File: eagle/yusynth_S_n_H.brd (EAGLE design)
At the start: 100.8 x 81 mm, 43 parts, among them IC1 TL074P, IC2 TL071P, Q1 BF245, T1 2N3904

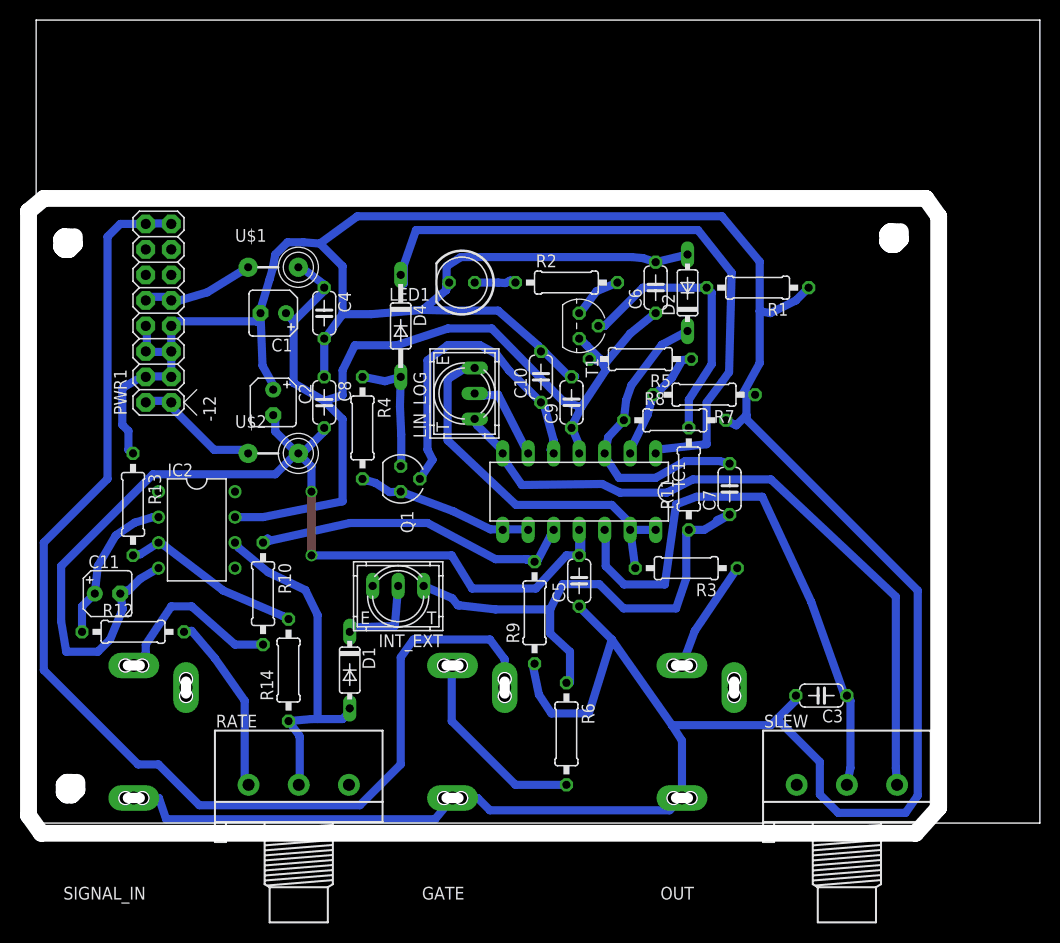
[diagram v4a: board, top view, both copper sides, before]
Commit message: adjusted a spacing, removed ridiculous bus gate and corrected pot reversals
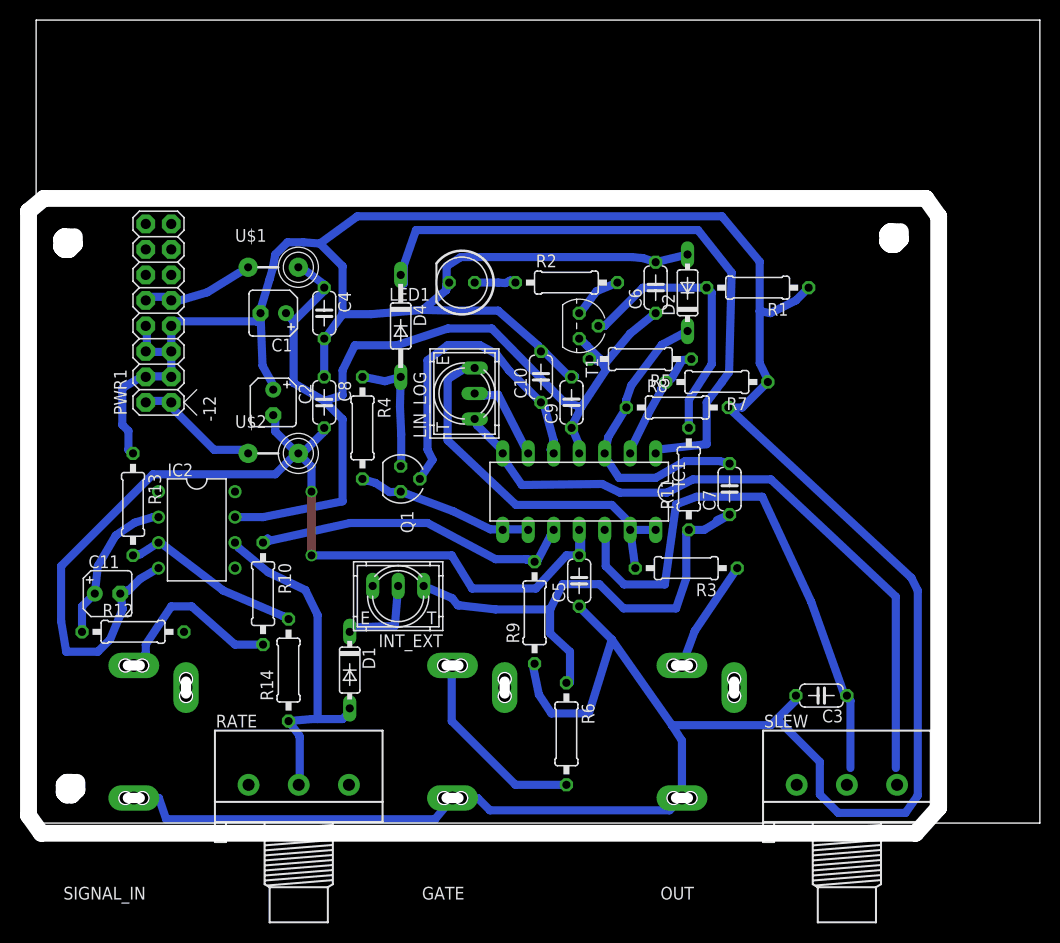
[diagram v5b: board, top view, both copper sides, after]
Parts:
- moved R7 1.80 mm to (67.8, 43.9)
- moved R8 1.30 mm to (63.9, 41.4)
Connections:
- removed net N$24: R12.2, RATE.1
- net N$12: now also R12.2, RATE.3; no longer GATE.P$2, PWR1.15, PWR1.16
- net N$19: now also SLEW.1; no longer SLEW.3
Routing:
- net N$12: track 121.3 -> 0.00 mm
- net N$24: track 18.0 -> 0.00 mm
- net N$13: track 57.7 -> 56.0 mm
- net N$19: track 69.5 -> 67.8 mm
- net N$7: track 11.8 -> 13.3 mm
- net GND: track 374.0 -> 372.6 mm
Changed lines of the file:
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@@
 <element name="R5" library="rcl" package="0207/10" value="100k" x="60.198" y="46.228" rot="R180"/>
 <element name="R6" library="rcl" package="0207/10" value="1k" x="52.832" y="8.89" rot="R270"/>
-<element name="R7" library="rcl" package="0207/10" value="10k" x="66.548" y="42.672" rot="R180"/>
-<element name="R8" library="rcl" package="0207/10" value="100k" x="63.627" y="40.132"/>
+<element name="R7" library="rcl" package="0207/10" value="10k" x="67.818" y="43.942" rot="R180"/>
+<element name="R8" library="rcl" package="0207/10" value="100k" x="63.881" y="41.402"/>
 <element name="R9" library="rcl" package="0207/10" value="100k" x="49.657" y="20.955" rot="R90"/>
 <element name="SLEW" library="pot" package="3RP/1610N" value="1M log" x="80.772" y="3.81"/>
@@
 <wire x1="28.2702" y1="57.7342" x2="26.6192" y2="57.8612" width="0.8128" layer="16"/>
 <wire x1="30.5308" y1="50.6984" x2="30.5308" y2="55.4736" width="0.8128" layer="16"/>
-<wire x1="70.4088" y1="42.7736" x2="72.0852" y2="45.8216" width="0.8128" layer="16"/>
-<wire x1="70.4088" y1="42.7736" x2="71.628" y2="42.672" width="0.8128" layer="16"/>
+<wire x1="72.9488" y1="44.0436" x2="72.0852" y2="45.8216" width="0.8128" layer="16"/>
+<wire x1="72.9488" y1="44.0436" x2="72.898" y2="43.942" width="0.8128" layer="16"/>
 <wire x1="63.3476" y1="9.7536" x2="57.3532" y2="18.288" width="0.8128" layer="16"/>
 <wire x1="57.3532" y1="18.288" x2="54.3052" y2="21.336" width="0.8128" layer="16"/>
@@
 <wire x1="55.0672" y1="10.922" x2="51.3334" y2="10.922" width="0.8128" layer="16"/>
 <wire x1="57.3532" y1="18.288" x2="55.0672" y2="10.922" width="0.8128" layer="16"/>
-<wire x1="70.7644" y1="40.2336" x2="70.7644" y2="40.64" width="0.8128" layer="16"/>
-<wire x1="70.7644" y1="40.64" x2="70.7644" y2="42.672" width="0.8128" layer="16"/>
-<wire x1="87.8332" y1="23.1648" x2="70.7644" y2="40.2336" width="0.8128" layer="16"/>
 <wire x1="87.8332" y1="2.7432" x2="87.8332" y2="23.1648" width="0.8128" layer="16"/>
 <wire x1="86.614" y1="1.016" x2="87.8332" y2="2.7432" width="0.8128" layer="16"/>
@@
 <wire x1="78.0796" y1="6.096" x2="78.0796" y2="2.8448" width="0.8128" layer="16"/>
 <wire x1="73.8124" y1="10.3632" x2="78.0796" y2="6.096" width="0.8128" layer="16"/>
-<wire x1="70.7644" y1="42.672" x2="71.628" y2="42.672" width="0.8128" layer="16"/>
 <wire x1="40.8432" y1="53.086" x2="40.8432" y2="53.594" width="0.8128" layer="16"/>
 <wire x1="40.8432" y1="53.594" x2="40.894" y2="53.6448" width="0.8128" layer="16"/>
@@
 <wire x1="68.326" y1="60.452" x2="32.004" y2="60.452" width="0.8128" layer="16"/>
 <wire x1="32.004" y1="60.452" x2="28.2702" y2="57.7342" width="0.8128" layer="16"/>
-<wire x1="68.707" y1="40.132" x2="69.7484" y2="39.624" width="0.8128" layer="16"/>
-<wire x1="69.7484" y1="39.624" x2="70.7644" y2="40.64" width="0.8128" layer="16"/>
+<wire x1="87.8332" y1="23.1648" x2="87.1982" y2="24.4348" width="0.8128" layer="16"/>
+<wire x1="87.1982" y1="24.4348" x2="68.961" y2="41.402" width="0.8128" layer="16"/>
 <wire x1="49.4538" y1="15.8496" x2="49.657" y2="15.875" width="0" layer="19" extent="16-16"/>
-</signal>
-<signal name="N$12">
-<contactref element="GATE" pad="P$2"/>
-<contactref element="PWR1" pad="15"/>
-<contactref element="PWR1" pad="16"/>
-<wire x1="13.462" y1="59.7408" x2="11.0236" y2="59.7408" width="0.8128" layer="16"/>
-<wire x1="11.0236" y1="59.7408" x2="10.922" y2="59.69" width="0.8128" layer="16"/>
-<wire x1="13.462" y1="59.7408" x2="13.462" y2="59.69" width="0.8128" layer="16"/>
-<wire x1="46.682" y1="13.5" x2="46.682" y2="16.31" width="0.8128" layer="16"/>
-<wire x1="46.682" y1="16.31" x2="45.212" y2="18.288" width="0.8128" layer="16"/>
-<wire x1="45.212" y1="18.288" x2="37.592" y2="18.288" width="0.8128" layer="16"/>
-<wire x1="37.592" y1="18.288" x2="36.322" y2="16.51" width="0.8128" layer="16"/>
-<wire x1="36.322" y1="16.51" x2="36.322" y2="5.842" width="0.8128" layer="16"/>
-<wire x1="36.322" y1="5.842" x2="32.258" y2="1.778" width="0.8128" layer="16"/>
-<wire x1="32.258" y1="1.778" x2="16.256" y2="1.778" width="0.8128" layer="16"/>
-<wire x1="16.256" y1="1.778" x2="12.192" y2="5.842" width="0.8128" layer="16"/>
-<wire x1="12.192" y1="5.842" x2="10.16" y2="5.842" width="0.8128" layer="16"/>
-<wire x1="10.16" y1="5.842" x2="0.762" y2="15.24" width="0.8128" layer="16"/>
-<wire x1="0.762" y1="15.24" x2="0.762" y2="27.94" width="0.8128" layer="16"/>
-<wire x1="0.762" y1="27.94" x2="7.112" y2="34.29" width="0.8128" layer="16"/>
-<wire x1="7.112" y1="34.29" x2="7.112" y2="58.42" width="0.8128" layer="16"/>
-<wire x1="7.112" y1="58.42" x2="8.382" y2="59.69" width="0.8128" layer="16"/>
-<wire x1="8.382" y1="59.69" x2="10.922" y2="59.69" width="0.8128" layer="16"/>
+<wire x1="68.961" y1="41.402" x2="70.358" y2="41.402" width="0.8128" layer="16"/>
+<wire x1="70.358" y1="41.402" x2="72.898" y2="43.942" width="0.8128" layer="16"/>
 </signal>
 <signal name="N$14">
@@
 <wire x1="59.182" y1="37.1348" x2="59.182" y2="36.83" width="0.8128" layer="16"/>
 <wire x1="60.9092" y1="40.64" x2="59.182" y2="37.1348" width="0.8128" layer="16"/>
-<wire x1="60.9092" y1="40.64" x2="61.468" y2="42.672" width="0.8128" layer="16"/>
+<wire x1="60.9092" y1="40.64" x2="62.738" y2="43.942" width="0.8128" layer="16"/>
 <wire x1="63.3476" y1="44.3484" x2="64.3636" y2="46.1264" width="0.8128" layer="16"/>
 <wire x1="62.2808" y1="43.2816" x2="63.3476" y2="44.3484" width="0.8128" layer="16"/>
 <wire x1="64.3636" y1="46.1264" x2="65.278" y2="46.228" width="0.8128" layer="16"/>
-<wire x1="62.2808" y1="43.2816" x2="61.468" y2="42.672" width="0.8128" layer="16"/>
+<wire x1="62.2808" y1="43.2816" x2="62.738" y2="43.942" width="0.8128" layer="16"/>
 </signal>
 <signal name="N$5">
@@
 <wire x1="56.9976" y1="38.4556" x2="56.7436" y2="37.1856" width="0.8128" layer="16"/>
 <wire x1="56.7436" y1="37.1856" x2="56.642" y2="36.83" width="0.8128" layer="16"/>
-<wire x1="56.9976" y1="38.4556" x2="58.547" y2="40.132" width="0.8128" layer="16"/>
+<wire x1="56.9976" y1="38.4556" x2="58.801" y2="41.402" width="0.8128" layer="16"/>
 <wire x1="64.6684" y1="36.068" x2="68.072" y2="36.068" width="0.8128" layer="16"/>
 <wire x1="61.722" y1="34.3916" x2="64.6684" y2="36.068" width="0.8128" layer="16"/>
@@
 <wire x1="58.7756" y1="42.1132" x2="59.2836" y2="43.5864" width="0.8128" layer="16"/>
 <wire x1="64.7192" y1="48.9204" x2="64.897" y2="49.022" width="0.8128" layer="16"/>
-<wire x1="58.7756" y1="42.1132" x2="58.547" y2="40.132" width="0.8128" layer="16"/>
+<wire x1="58.7756" y1="42.1132" x2="58.801" y2="41.402" width="0.8128" layer="16"/>
 </signal>
 <signal name="N$4">
@@
 <signal name="N$13">
 <contactref element="IC1" pad="12"/>
-<contactref element="SLEW" pad="2"/>
 <contactref element="C3" pad="1"/>
 <wire x1="81.1276" y1="5.4864" x2="81.1276" y2="12.192" width="0.8128" layer="16"/>
 <wire x1="81.1276" y1="12.192" x2="80.772" y2="12.7" width="0.8128" layer="16"/>
-<wire x1="81.1276" y1="5.4864" x2="80.772" y2="3.81" width="0.8128" layer="16"/>
 <wire x1="56.7436" y1="25.6032" x2="56.7436" y2="28.6512" width="0.8128" layer="16"/>
 <wire x1="58.5724" y1="23.7744" x2="56.7436" y2="25.6032" width="0.8128" layer="16"/>
@@
 <wire x1="56.7436" y1="28.6512" x2="56.642" y2="29.21" width="0.8128" layer="16"/>
 <wire x1="80.518" y1="12.8016" x2="80.772" y2="12.7" width="0.8128" layer="16"/>
+<contactref element="SLEW" pad="2"/>
+<wire x1="80.772" y1="3.81" x2="81.1276" y2="5.4864" width="0" layer="19" extent="16-16"/>
 </signal>
 <signal name="N$19">
-<contactref element="SLEW" pad="3"/>
 <contactref element="IC1" pad="7"/>
 <contactref element="LIN_LOG" pad="1"/>
@@
 <wire x1="58.166" y1="32.9184" x2="62.8396" y2="32.9184" width="0.8128" layer="16"/>
 <wire x1="46.3804" y1="36.576" x2="48.387" y2="33.6804" width="0.8128" layer="16"/>
-<wire x1="85.6488" y1="5.4864" x2="85.772" y2="3.81" width="0.8128" layer="16"/>
 <wire x1="46.3804" y1="36.576" x2="46.482" y2="36.83" width="0.8128" layer="16"/>
+<contactref element="SLEW" pad="1"/>
+<wire x1="75.772" y1="3.81" x2="85.6488" y2="5.4864" width="0" layer="19" extent="16-16"/>
 </signal>
 <signal name="N$20">
@@
 <wire x1="4.572" y1="21.59" x2="5.842" y2="22.86" width="0.8128" layer="16"/>
 </signal>
-<signal name="N$24">
-<contactref element="R12" pad="2"/>
-<contactref element="RATE" pad="1"/>
-<wire x1="17.78" y1="16.4592" x2="15.494" y2="19.1516" width="0.8128" layer="16"/>
-<wire x1="20.7772" y1="12.192" x2="17.78" y2="16.4592" width="0.8128" layer="16"/>
-<wire x1="20.7772" y1="4.2672" x2="20.7772" y2="12.192" width="0.8128" layer="16"/>
-<wire x1="15.494" y1="19.1516" x2="14.732" y2="19.05" width="0.8128" layer="16"/>
-<wire x1="20.7772" y1="4.2672" x2="21.162" y2="3.81" width="0.8128" layer="16"/>
-</signal>
 <signal name="N$25">
 <contactref element="D1" pad="A"/>
 <contactref element="IC2" pad="6"/>
-<contactref element="RATE" pad="2"/>
 <contactref element="R14" pad="1"/>
 <wire x1="30.5308" y1="10.3632" x2="28.0416" y2="10.3632" width="0.8128" layer="16"/>
@@
 <wire x1="26.2636" y1="8.5344" x2="26.2636" y2="4.2672" width="0.8128" layer="16"/>
 <wire x1="26.2128" y1="8.7376" x2="26.2636" y2="8.5344" width="0.8128" layer="16"/>
-<wire x1="26.2636" y1="4.2672" x2="26.162" y2="3.81" width="0.8128" layer="16"/>
 <wire x1="26.2128" y1="8.7376" x2="25.146" y2="10.16" width="0.8128" layer="16"/>
+<contactref element="RATE" pad="2"/>
+<wire x1="26.162" y1="3.81" x2="26.2636" y2="4.2672" width="0" layer="19" extent="16-16"/>
 </signal>
 <signal name="N$22">
@@
 <wire x1="31.1404" y1="19.5072" x2="31.242" y2="19.05" width="0.8128" layer="16"/>
 </signal>
+<signal name="N$12">
+<contactref element="RATE" pad="3"/>
+<contactref element="R12" pad="2"/>
+<wire x1="14.732" y1="19.05" x2="31.162" y2="3.81" width="0" layer="19" extent="1-1"/>
+</signal>
 </signals>
